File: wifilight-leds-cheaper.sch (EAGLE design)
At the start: 53 parts, among them Q1 BUK98180-100A, Q2 BUK98180-100A, Q3 BUK98180-100A, Q4 BUK98180-100A, U2 PCA9685

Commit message: Swapped to using 12x Luxeon Rebels instead of the hard-to-solder consolidated package.
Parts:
- removed C3: 220pf, resistor:C-EUC0805K
- removed C4: 0.1uF, resistor:C-EUC0805K
- removed D1: MBRS140T3, diode:MBRS130LT3
- removed H1: SEW_HOLE, LilyPad-Wearables:SEW_HOLE
- removed L1: 220uf, SparkFun-Passives:INDUCTORSDR0403-560KL
- removed LED1, LED2, LED3: OVSTRGBBCR8, led:OVSTRGBBCR8
- removed R1: 220 ???, resistor:R-EU_R0805
- removed R3: 3K, resistor:R-EU_R0805
- removed R4: 1K, resistor:R-EU_R0805
- removed REG1: MC33063/MC34063D, adafruit:MC33063/MC34063D
- removed TEMPERATURE: MPL3115A2LGA8, SparkFun-Sensors:MPL3115A2LGA8
- removed TP5V: TEST-POINT3X5, SparkFun-Passives:TEST-POINT3X5
- added BL1, BL2, BL3, GL1, GL2, GL3, RL1, RL2, RL3: LUXEON-REBEL, SparkFun-LED:LUXEON-REBEL
- added JP2: (no value), SparkFun-Connectors:M05X2SHD_LOCK
- renumbered U$1 to WL3, U$2 to WL2, U$3 to WL1
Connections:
- net N$10 renamed W1
- net N$11 renamed W2
- net N$20 renamed #OE
- removed net 5V: C5.+, C6.1, L1.1, R3.1, REG2.IN, TP5V.1
- removed net COMP: R3.2, R4.1, REG1.COMP
- removed net N$1: LED1-G.C, LED2-G.A
- removed net N$13: R1.2, REG1.DC, REG1.IPK, REG1.SWC
- removed net N$16: C3.1, REG1.TC
- removed net N$17: C4.1, TEMPERATURE.CAP
- removed net N$2: LED2-G.C, LED3-G.A
- removed net N$5: LED2-R.C, LED3-R.A
- removed net N$6: LED1-R.C, LED2-R.A
- removed net N$7: LED1G$1.C, LED2G$1.A
- removed net N$8: LED2G$1.C, LED3G$1.A
- removed net SWE: D1.C, L1.2, REG1.SWE
- new net B1: BL2.A, BL3.C
- new net B2: BL1.A, BL2.C
- new net G1: GL2.A, GL3.C
- new net G2: GL1.A, GL2.C
- new net R1: RL2.A, RL3.C
- new net R2: RL1.A, RL2.C
- net 12V: now also BL3.A, C5.+, C6.1, GL3.A, JP2.1, REG2.IN, RL3.A; no longer LED1-G.A, LED1-R.A, LED1G$1.A, R1.1, REG1.VCC
- net 3.3V: now also JP2.5; no longer TEMPERATURE.VDD, TEMPERATURE.VDDIO
- net BLUE: now also U2.PWM0; no longer U2.PWM1
- net CH_PD: now also JP2.10
- net GND: now also BL1.S, BL2.S, BL3.S, GL1.S, GL2.S, GL3.S, JP2.3, RL1.S, RL2.S, RL3.S; no longer C3.2, C4.2, D1.A, H1.P$1, R4.2, REG1.GND, TEMPERATURE.GND
- net GPIO0: now also JP2.6
- net GPIO2: now also JP2.8
- net GREEN: now also U2.PWM1; no longer U2.PWM3
- net P_BLUE: now also BL1.C; no longer LED3G$1.C
- net P_GREEN: now also GL1.C; no longer LED3-G.C
- net P_RED: now also RL1.C; no longer LED3-R.C
- net RXD: now also JP2.4
- net SCL: now also JP2.7; no longer TEMPERATURE.SDA
- net SDA: now also JP2.9; no longer TEMPERATURE.SCL
- net TXD: now also JP2.2
- net WHITE: now also U2.PWM3; no longer U2.PWM0
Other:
- moved on the sheet: C1, C2

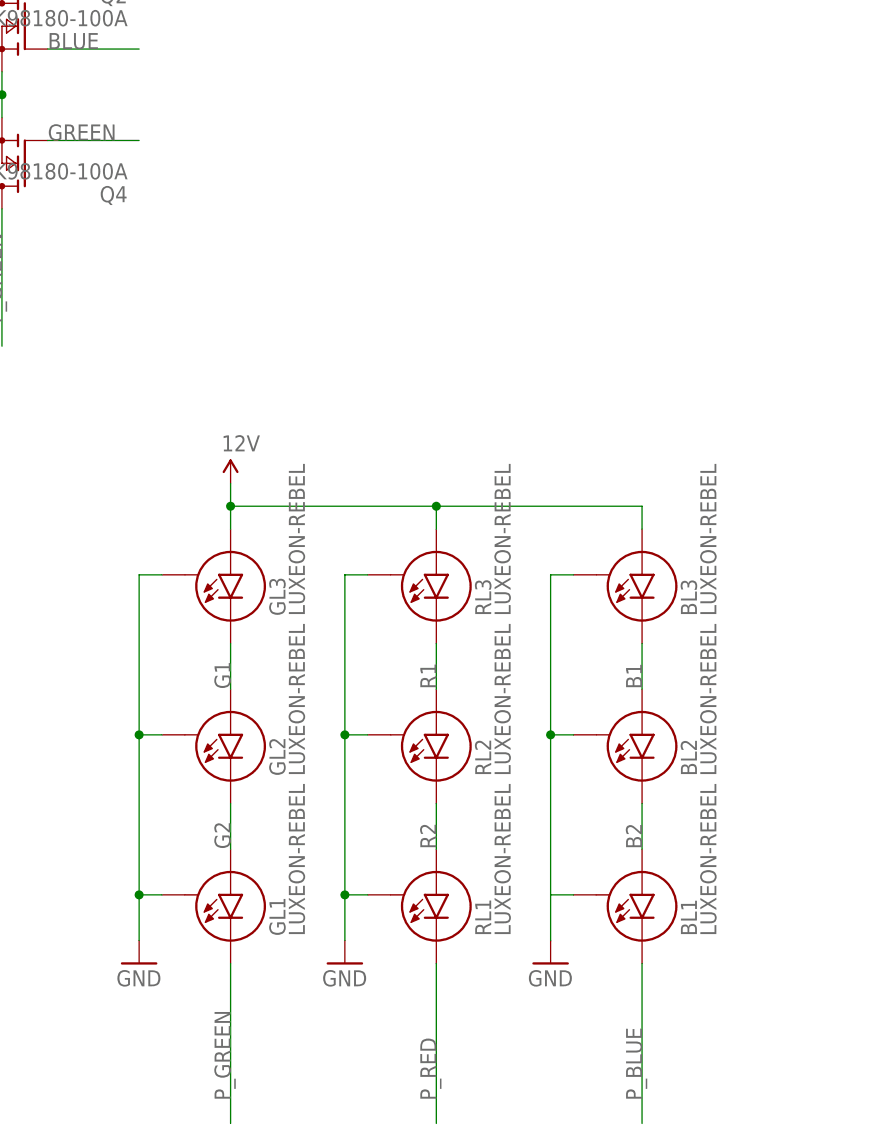
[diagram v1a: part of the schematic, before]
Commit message: Rotate socket to allow it not to clip through one of the SOT-223 transitors
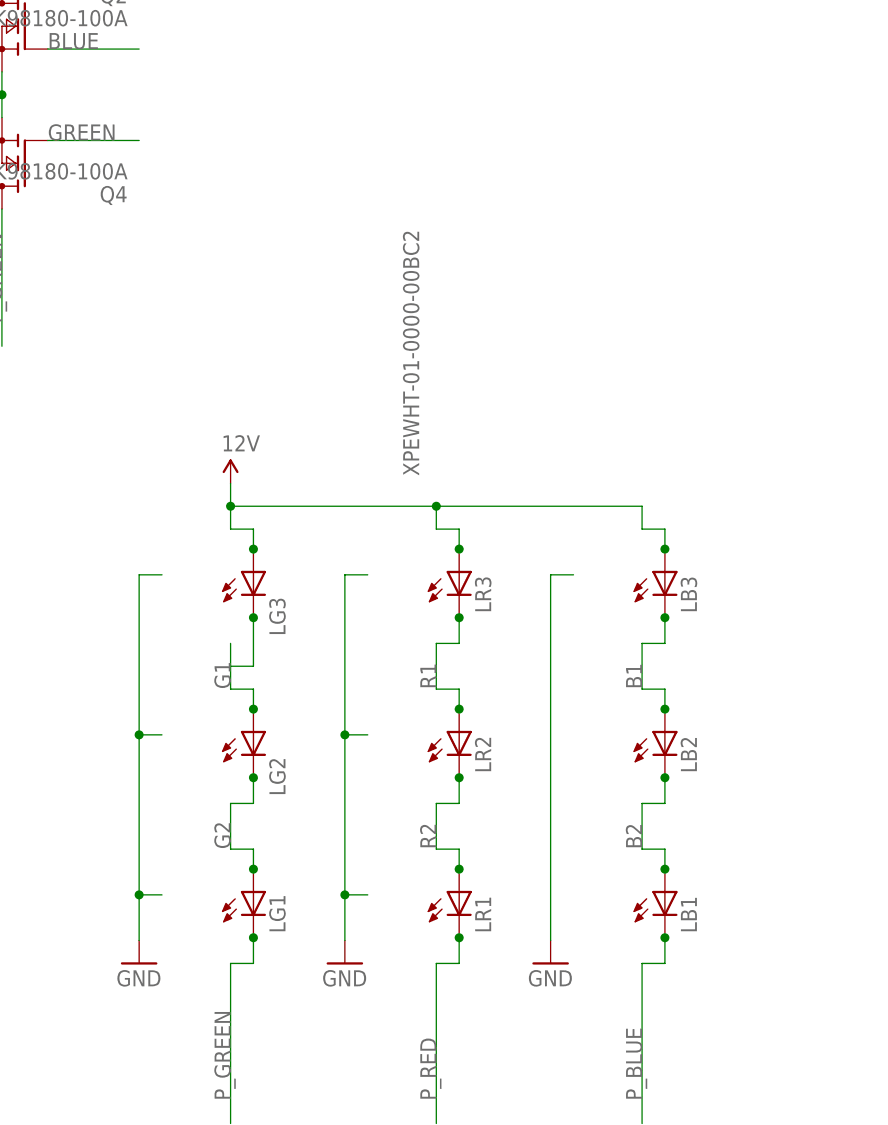
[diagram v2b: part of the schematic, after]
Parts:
- removed BL1, BL2, BL3, GL1, GL2, GL3, RL1, RL2, RL3: LUXEON-REBEL, SparkFun-LED:LUXEON-REBEL
- added LB1, LB2, LB3, LG1, LG2, LG3, LR1, LR2, LR3: XPEWHT-01-0000-00BC2, led:XPEWHT-01-0000-00BC2
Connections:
- net 12V: now also LB3.A, LG3.A, LR3.A; no longer BL3.A, GL3.A, RL3.A
- net B1: now also LB2.A, LB3.C; no longer BL2.A, BL3.C
- net B2: now also LB1.A, LB2.C; no longer BL1.A, BL2.C
- net G1: now also LG2.A, LG3.C; no longer GL2.A, GL3.C
- net G2: now also LG1.A, LG2.C; no longer GL1.A, GL2.C
- net GND: no longer BL1.S, BL2.S, BL3.S, GL1.S, GL2.S, GL3.S, RL1.S, RL2.S, RL3.S
- net P_BLUE: now also LB1.C; no longer BL1.C
- net P_GREEN: now also LG1.C; no longer GL1.C
- net P_RED: now also LR1.C; no longer RL1.C
- net R1: now also LR2.A, LR3.C; no longer RL2.A, RL3.C
- net R2: now also LR1.A, LR2.C; no longer RL1.A, RL2.C

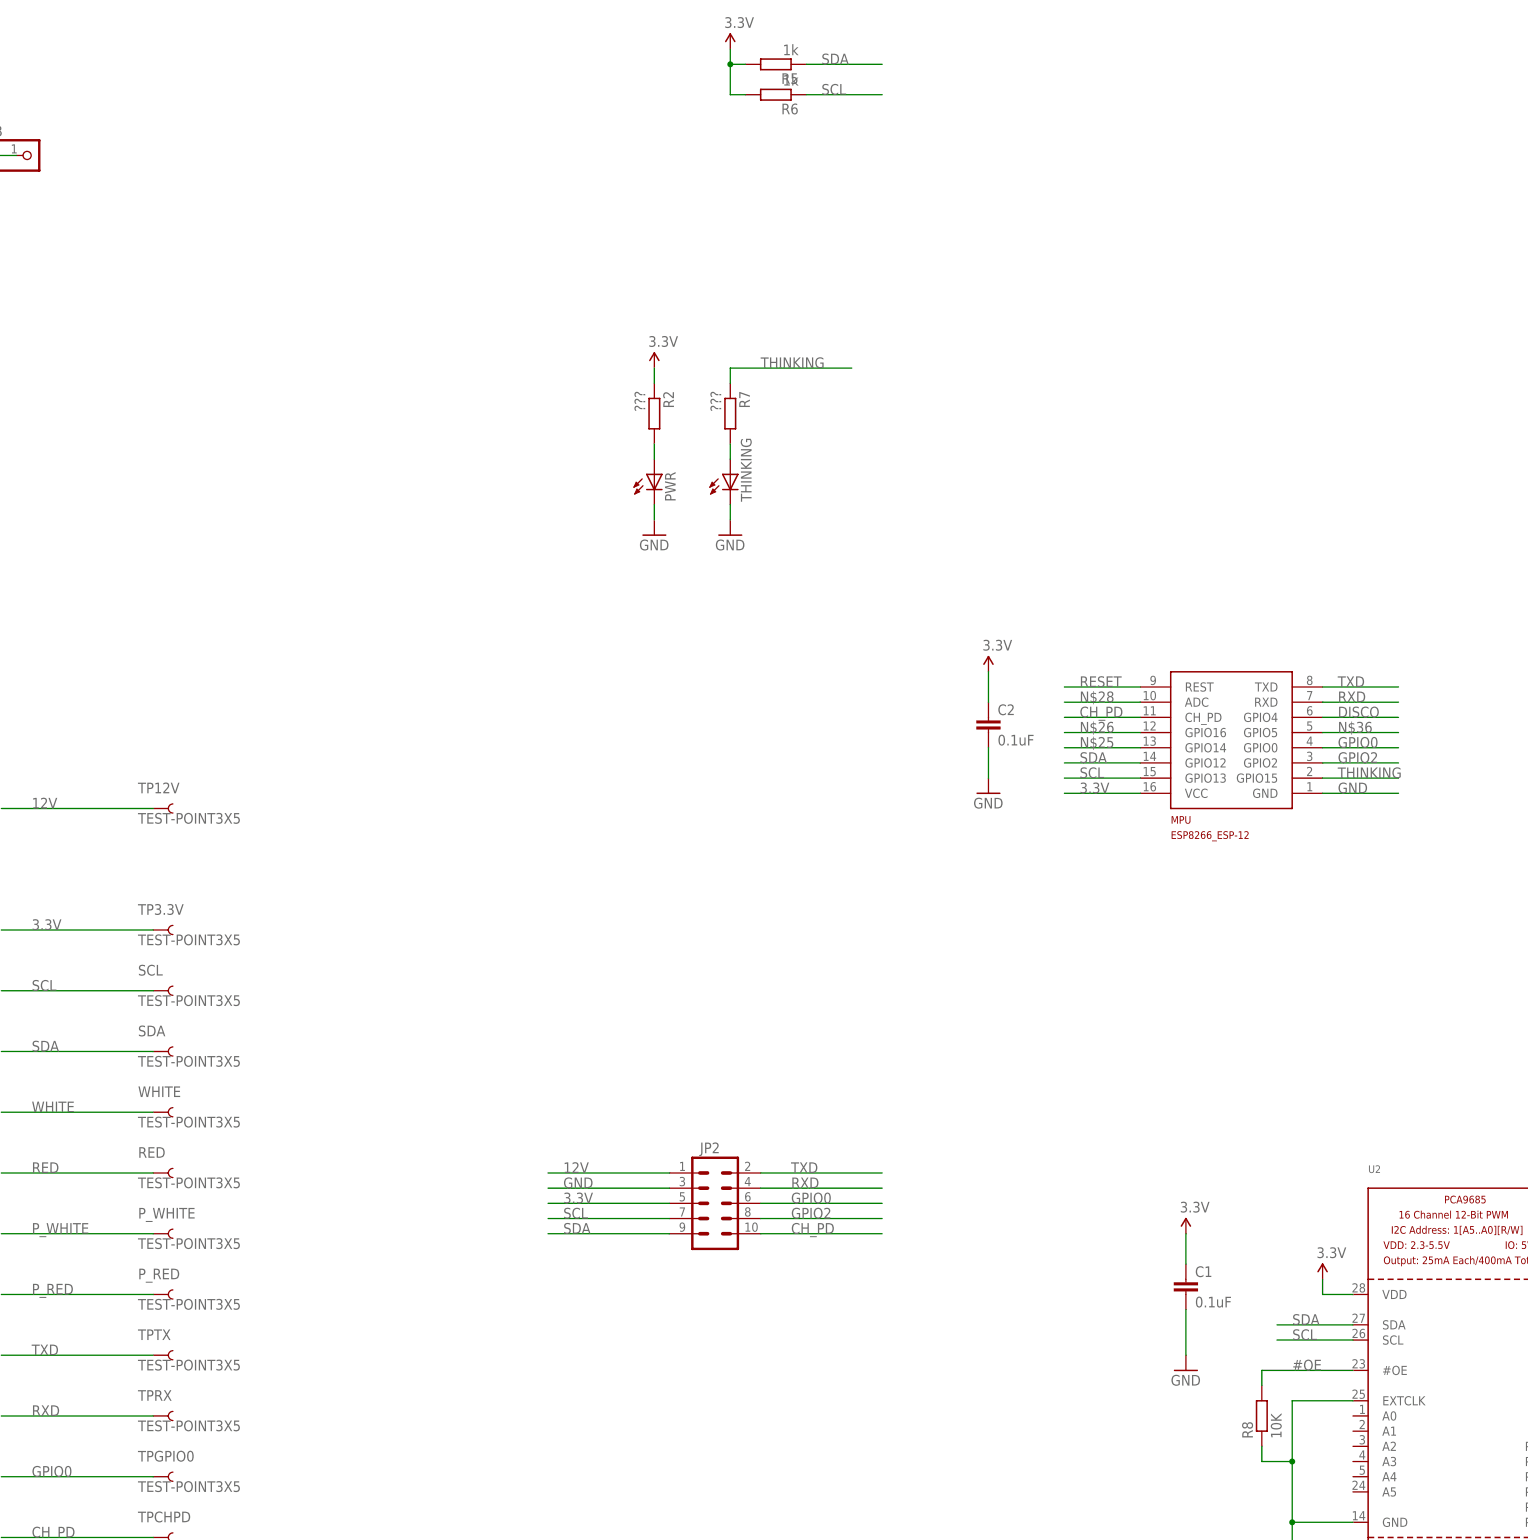
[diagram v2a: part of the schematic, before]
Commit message: Adding more signals to a better connector, moved THINKING LED to another GPIO due to conflict
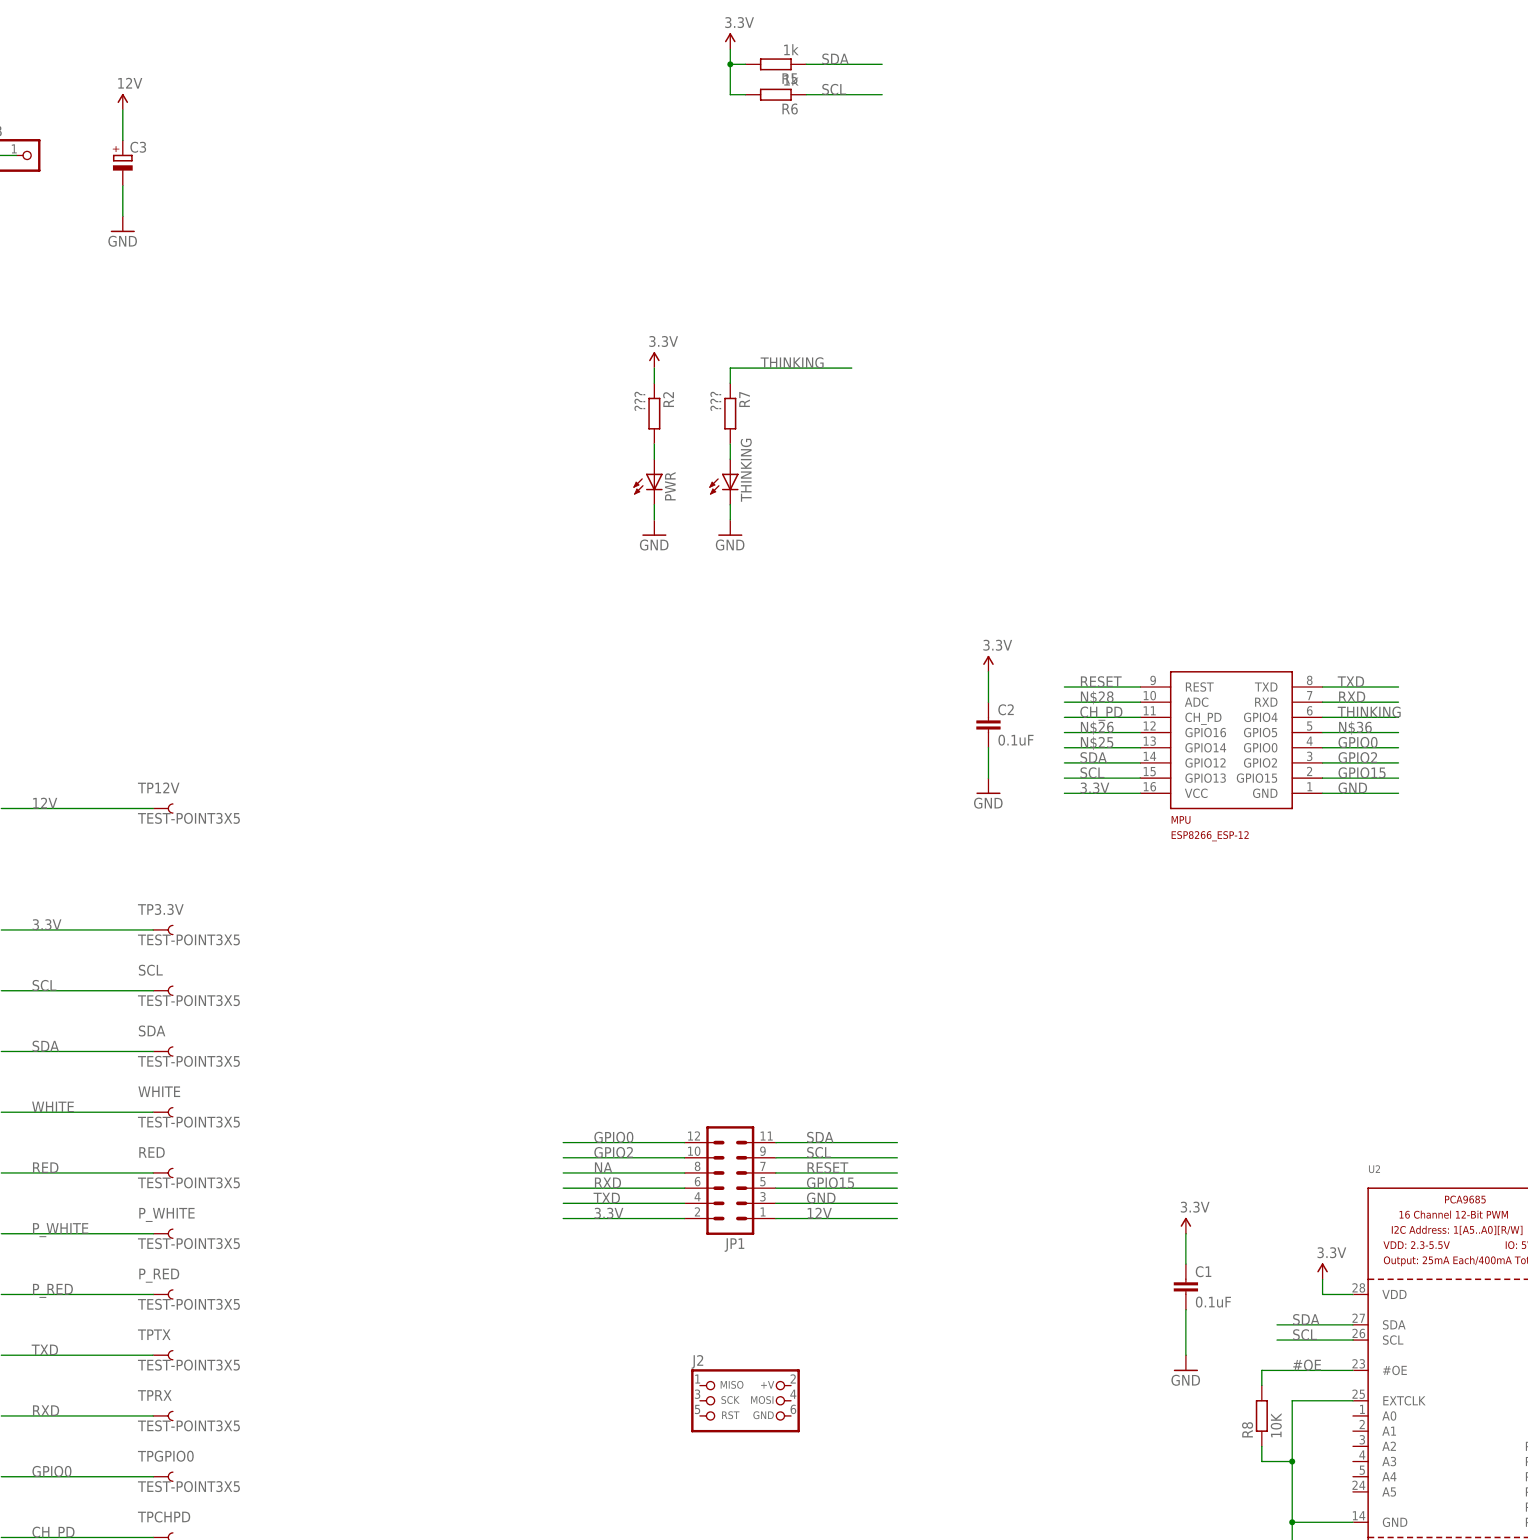
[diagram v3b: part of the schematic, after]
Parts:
- removed JP2: (no value), SparkFun-Connectors:M05X2SHD_LOCK
- added C3: (no value), rcl:CPOL-EUE3.5-8
- added J2: CON_HEADER_PRG_AVR_ICSP-PTH, dp_devices:CON_HEADER_PRG_AVR_ICSP-PTH
- added JP1: (no value), SparkFun-Connectors:M06X2FEMALE-SMT
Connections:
- removed net DISCO: MPU.GPIO4
- new net GPIO15: JP1.5, MPU.GPIO15
- new net NA: JP1.8
- net 12V: now also C3.+, JP1.1; no longer JP2.1
- net 3.3V: now also JP1.2; no longer JP2.5
- net CH_PD: no longer JP2.10
- net GND: now also C3.-, JP1.3; no longer JP2.3
- net GPIO0: now also JP1.12; no longer JP2.6
- net GPIO2: now also JP1.10; no longer JP2.8
- net RESET: now also JP1.7
- net RXD: now also JP1.6; no longer JP2.4
- net SCL: now also JP1.9; no longer JP2.7
- net SDA: now also JP1.11; no longer JP2.9
- net THINKING: now also MPU.GPIO4; no longer MPU.GPIO15
- net TXD: now also JP1.4; no longer JP2.2
